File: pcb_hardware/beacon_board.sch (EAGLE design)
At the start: 19 parts, among them IC1-AVR ATMEGA32U4TQFP, J1-ISP AVR_SPI_PRG_6PTH, Y1 16MHz

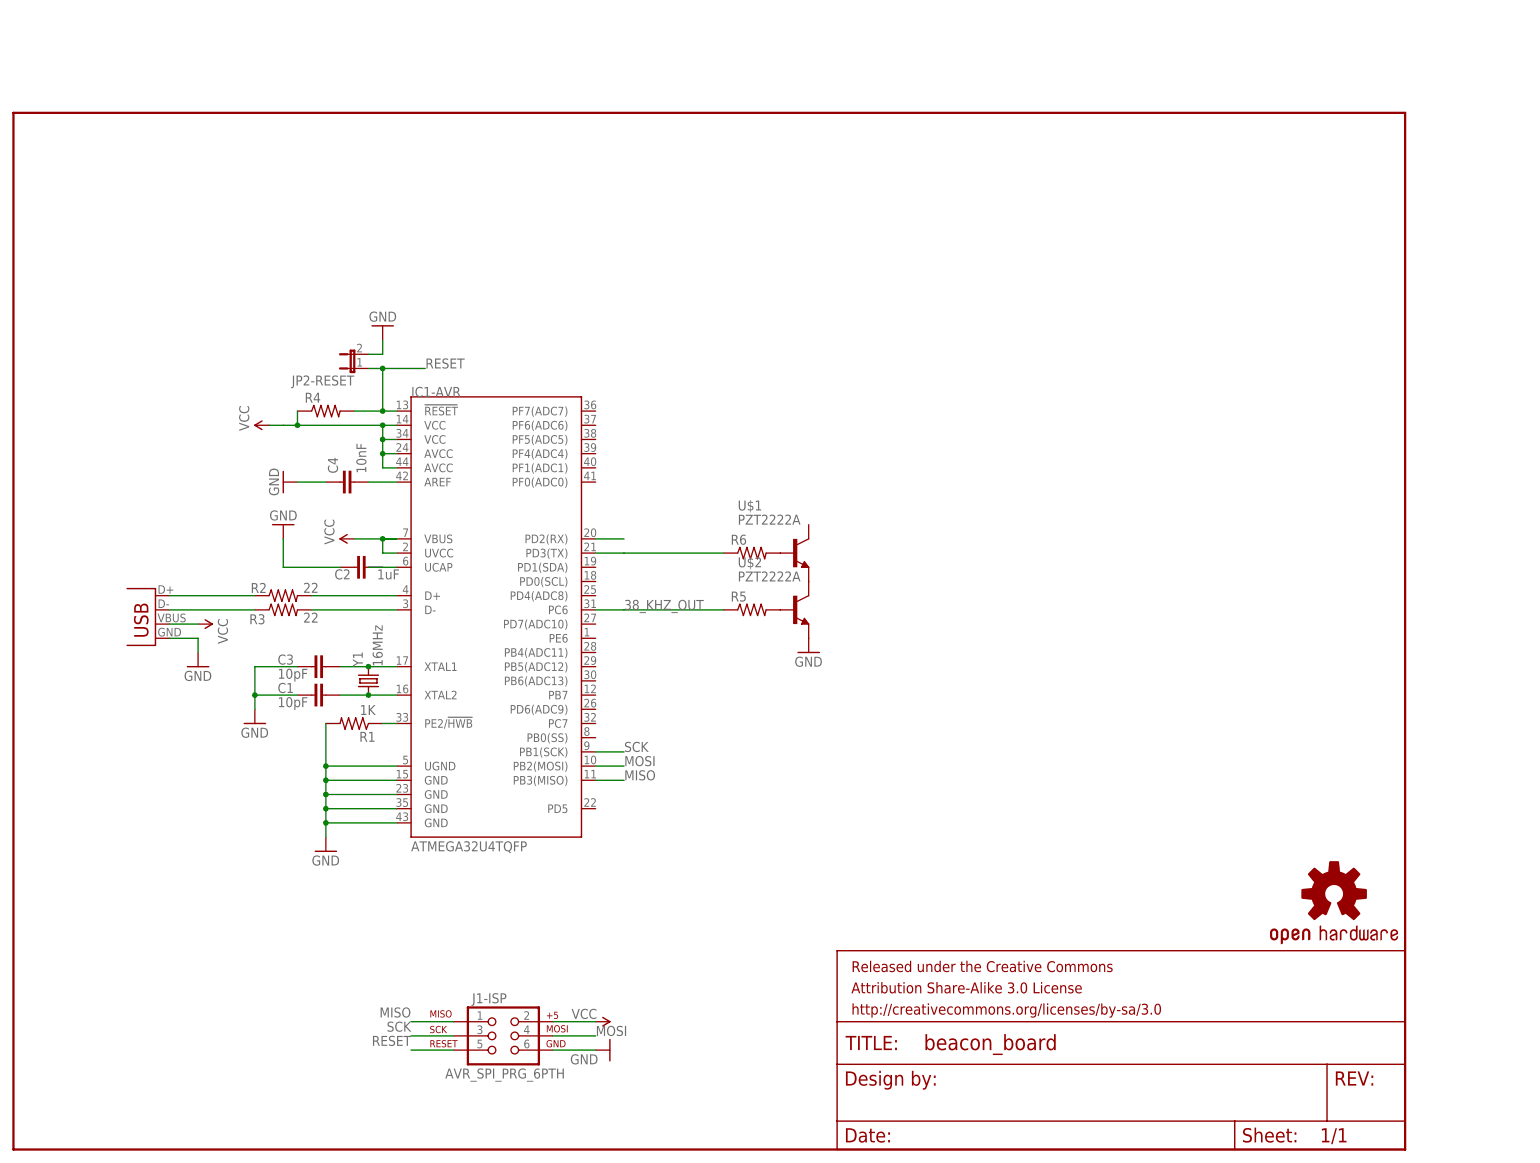
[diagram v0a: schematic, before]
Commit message: Finish initial unchecked schematic capture
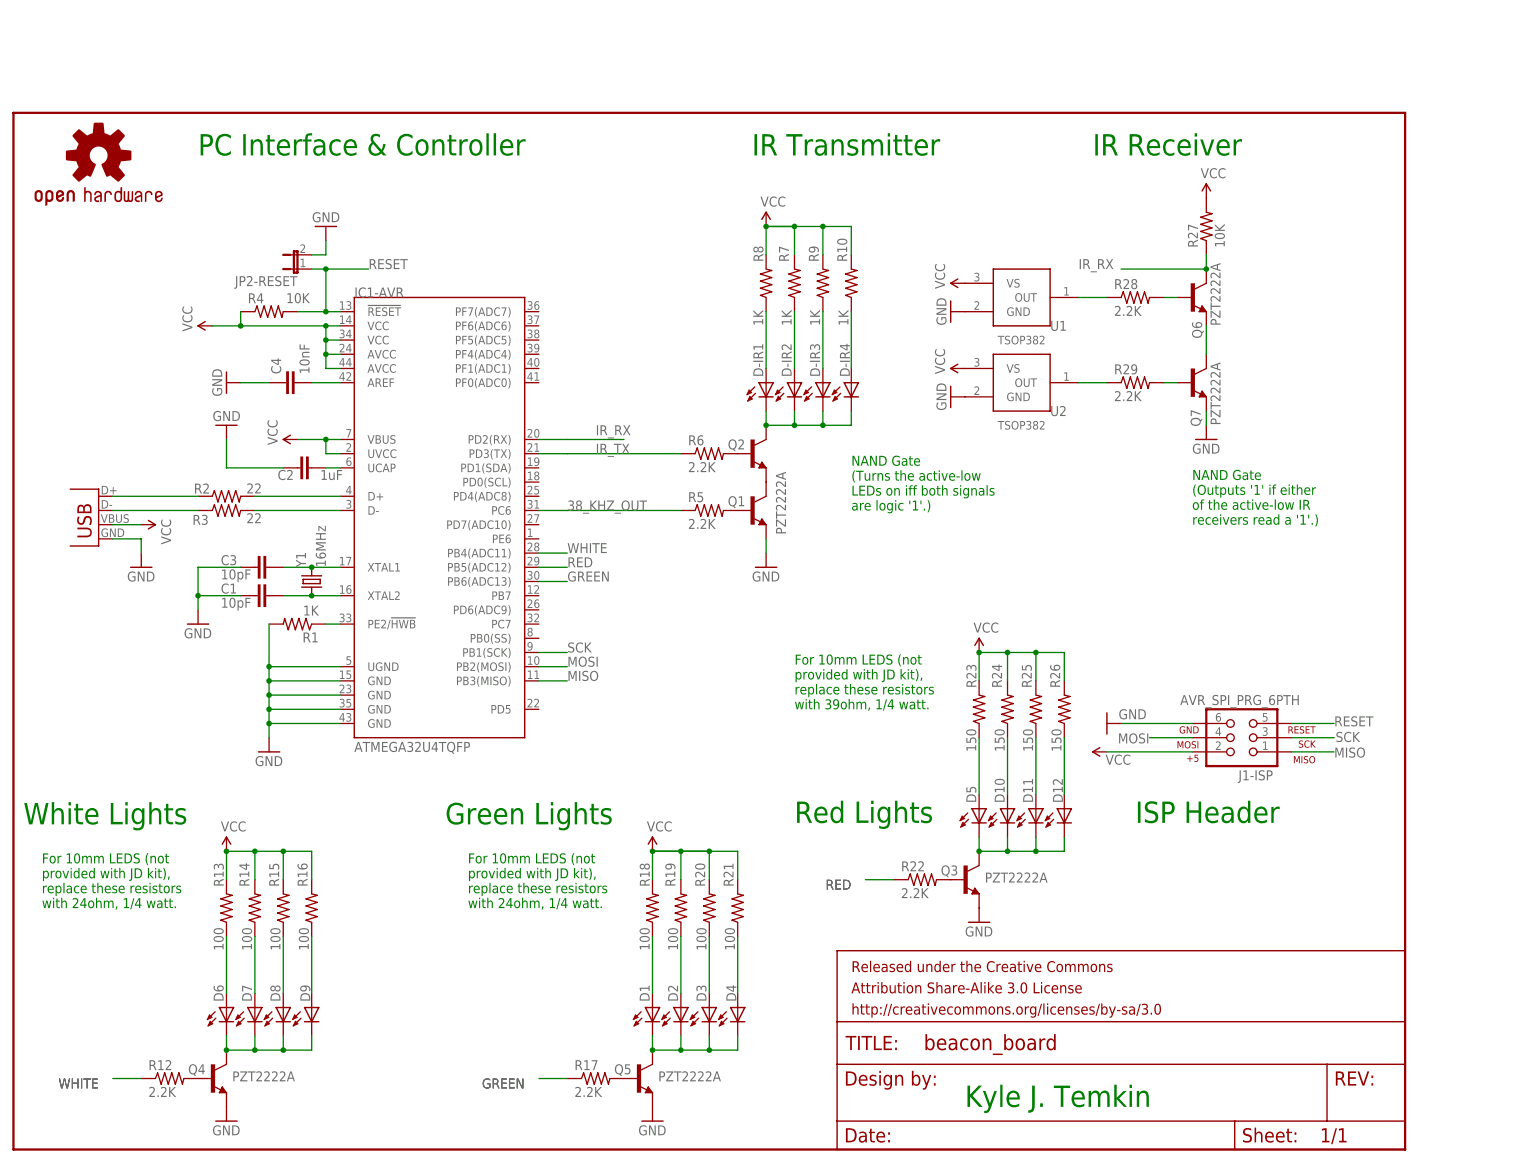
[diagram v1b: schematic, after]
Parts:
- removed U$2: PZT2222A, junior_design:PZT2222A
- added D-IR1, D-IR2, D-IR3, D-IR4: (no value), SparkFun-LED:LED5MM
- added D1, D10, D11, D12, D2, D3, D4, D5, D6, D7, D8, D9: (no value), SparkFun-LED:LED10MM
- added Q1, Q2, Q3, Q4, Q5, Q6, Q7: PZT2222A, junior_design:PZT2222A
- added R10, R7, R8, R9: 1K, SparkFun-Resistors:RESISTOR0805-RES
- added R12, R17, R22, R28, R29: 2.2K, SparkFun-Resistors:RESISTOR0805-RES
- added R13, R14, R15, R16, R18, R19, R20, R21: 100, SparkFun-Resistors:RESISTOR0805-RES
- added R23, R24, R25, R26: 150, SparkFun-Resistors:RESISTOR0805-RES
- added R27: 10K, SparkFun-Resistors:RESISTOR0805-RES
- added U1, U2: (no value), junior_design:TSOP382
- R4: value (none) -> 10K
- R5, R6: value (none) -> 2.2K
- U$1: value PZT2222A -> BINGHAMTON-EECE-TEXT; device junior_design:PZT2222A -> logos:BINGHAMTON-EECE-TEXT
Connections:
- net N$9 renamed IR_TX
- new net D1: D1.C, D2.C, D3.C, D4.C, Q5.C
- new net D2: D10.C, D11.C, D12.C, D5.C, Q3.C
- new net D9: D6.C, D7.C, D8.C, D9.C, Q4.C
- new net GREEN: IC1-AVR.PB6(ADC13), R17.1
- new net IR_RX: IC1-AVR.PD2(RX), Q6.C, R27.1
- new net N$15: D-IR1.C, D-IR2.C, D-IR3.C, D-IR4.C, Q2.C
- new net N$16: D-IR1.A, R8.1
- new net N$17: D1.A, R18.1
- new net N$18: D6.A, R13.1
- new net N$19: D-IR3.A, R9.1
- new net N$20: D8.A, R15.1
- new net N$21: D3.A, R20.1
- new net N$22: Q3.B, R22.2
- new net N$23: D5.A, R23.1
- new net N$24: D11.A, R25.1
- new net N$25: Q6.E, Q7.C
- new net N$26: R28.1, U1.OUT
- new net N$27: Q6.B, R28.2
- new net N$28: Q7.B, R29.2
- new net N$29: R29.1, U2.OUT
- new net N$9: Q4.B, R12.2
- new net RED: IC1-AVR.PB5(ADC12), R22.1
- new net VCC1: D-IR2.A, R7.1
- new net VCC2: D7.A, R14.1
- new net VCC3: D-IR4.A, R10.1
- new net VCC4: D9.A, R16.1
- new net VCC5: D2.A, R19.1
- new net VCC6: D4.A, R21.1
- new net VCC7: D10.A, R24.1
- new net VCC8: D12.A, R26.1
- new net WHITE: IC1-AVR.PB4(ADC11), R12.1
- net GND: now also Q1.E, Q3.E, Q4.E, Q5.E, Q7.E, U1.GND, U2.GND; no longer U$2.E
- net N$10: now also Q5.B, R17.2; no longer IC1-AVR.PD2(RX)
- net N$12: now also Q2.B; no longer U$1.B
- net N$13: now also Q1.B; no longer U$2.B
- net N$14: now also Q1.C, Q2.E; no longer U$1.E, U$2.C
- net VCC: now also R10.2, R13.2, R14.2, R15.2, R16.2, R18.2, R19.2, R20.2, R21.2, R23.2, R24.2, R25.2, R26.2, R27.2, R7.2, R8.2, R9.2, U1.VS, U2.VS
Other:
- note added: "For 10mm LEDS (not provided with JD kit), replace these resistors with 24ohm, 1/4 watt."
- note added: "For 10mm LEDS (not provided with JD kit), replace these resistors with 39ohm, 1/4 watt."
- note added: "Green Lights"
- note added: "IR Receiver"
- note added: "IR Transmitter"
- note added: "ISP Header"
- note added: "Kyle J. Temkin"
- note added: "NAND Gate (Outputs '1' if either of the active-low IR receivers read a '1'.)"
- note added: "NAND Gate (Turns the active-low LEDs on iff both signals are logic '1'.)"
- note added: "PC Interface & Controller"
- note added: "Red Lights"
- note added: "White Lights"
- moved on the sheet: C1, C2, C3, C4, IC1-AVR, J1-ISP, JP2-RESET, R1, R2, R3, R4, R5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

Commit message: Add scratch work for board layout
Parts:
- added C5: 1uF, SparkFun-Passives:CAP0805
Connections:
- net D2: now also D9.C; no longer D5.C
- net D9: now also D5.C; no longer D9.C
- net GND: now also C5.2
- net N$18: now also D5.A; no longer D6.A
- net N$20: now also D7.A; no longer D8.A
- net N$23: now also D9.A; no longer D5.A
- net VCC: now also C5.1
- net VCC2: now also D6.A; no longer D7.A
- net VCC4: now also D8.A; no longer D9.A
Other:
- moved on the sheet: D5, D6, D7, D8, D9

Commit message: Complete alpha prototype for PCB
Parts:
- removed FRAME1: FRAME-LETTER, SparkFun-Aesthetics:FRAME-LETTER
- added R11, R30, R31, R32: 1K, SparkFun-Passives:RESISTOR0805-RES
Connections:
- new net N$30: R11.2, R30.2, R31.2, R32.2
- new net N$31: R11.1, R30.1, R31.1, R32.1
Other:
- note added: "If you are already comfortable with SMT soldering, you may skip populating these resistors."
- note added: "JD Beacon Board"
- note added: "R0-8-20-13-KT"
- note added: "Soldering Practice"
- moved on the sheet: C1, C2, C3, C4, C5, D-IR1, D-IR2, D-IR3, D-IR4, D1, D10, D11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
